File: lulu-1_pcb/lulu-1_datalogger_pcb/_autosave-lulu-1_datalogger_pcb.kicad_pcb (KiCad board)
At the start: 2 copper layers, 100.5 x 30.5 mm, 51 parts, among them J1 B2B-XH-A, J2 SBH11-PBPC-D10-ST-BK, J3 MEM2067-02-180-00-A_REVB, SW1 SW_Nidec_CAS-120A1, U1 STM32F401RETx, U2 BAT54LT1G, U3 LP3982ILD-3.3, U4 BMP280, U5 MPU-6050, U6 W25Q16JVSS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

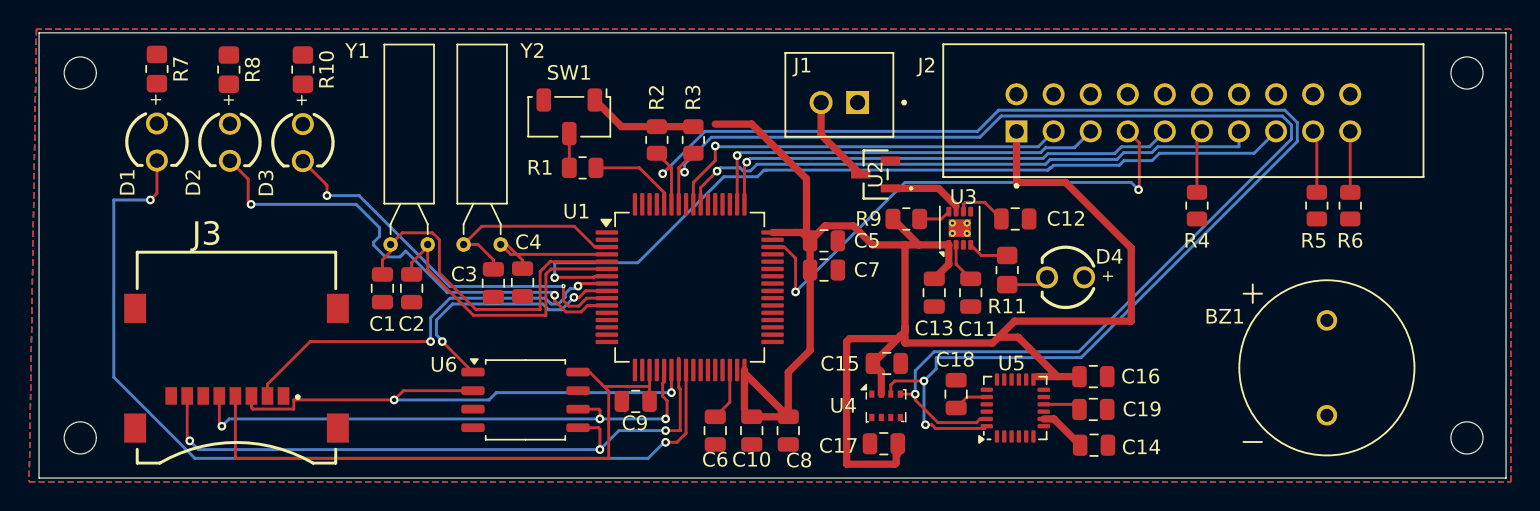
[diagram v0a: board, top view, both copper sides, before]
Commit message: changed clearance to 0.15mm
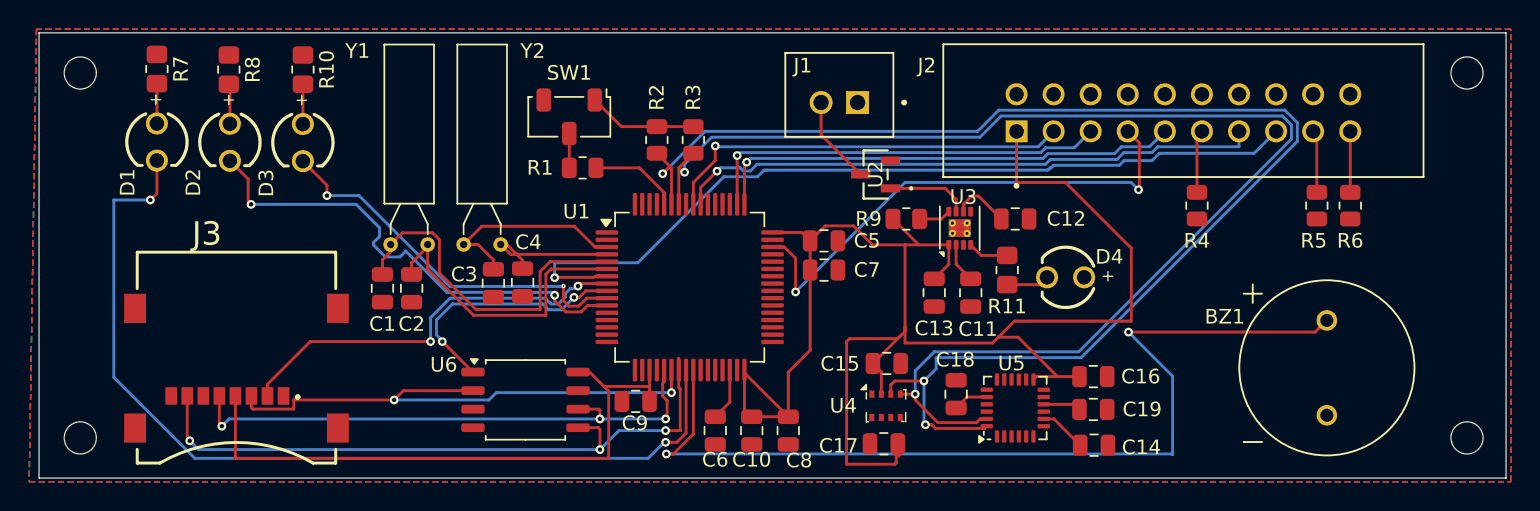
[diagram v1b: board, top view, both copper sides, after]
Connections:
- BZ1 pad N: (no net) -> GND
- BZ1 pad P: (no net) -> BUZZ
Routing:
- net BUZZ: track 0.00 -> 65.0 mm, vias 0 -> 2
- net +3V3: track 174.4 -> 162.6 mm
- net Net-(D2-K): track 0.00 -> 2.74 mm
- net Net-(D3-K): track 0.00 -> 2.73 mm
- net Net-(D1-K): track 0.00 -> 2.73 mm

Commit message: resolved all DRC errors
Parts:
- moved C8 1.26 mm to (149.4, 140.4)
- moved C10 1.16 mm to (147.2, 140.4)
- moved C6 1.15 mm to (145.0, 140.3)
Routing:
- net GND: track 0.00 -> 91.9 mm, vias 0 -> 4
- net +3V3: track 162.6 -> 234.2 mm, vias 0 -> 4
- net VBUS: track 14.5 -> 31.9 mm, vias 0 -> 2
- net Net-(U1-VCAP1): track 3.61 -> 2.46 mm
